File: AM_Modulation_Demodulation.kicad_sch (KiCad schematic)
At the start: 33 parts, among them U1 LM1496H, U2 TL082

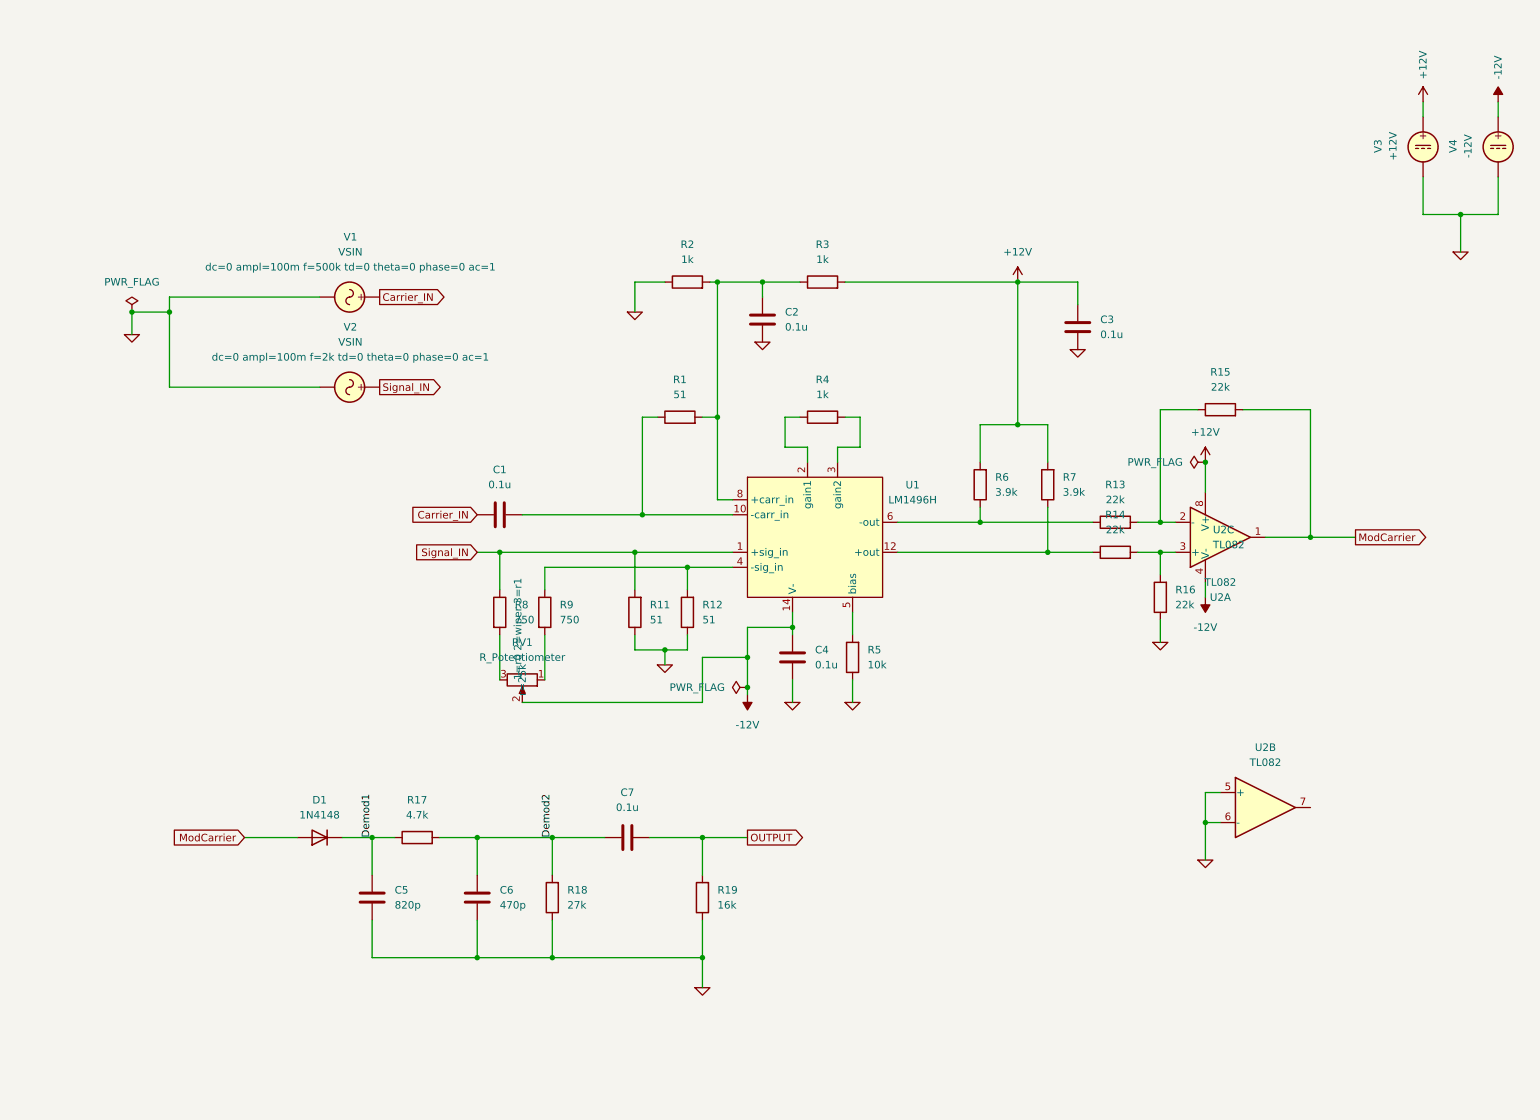
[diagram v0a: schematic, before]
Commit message: Rearranged Schematic. Fixed Readme
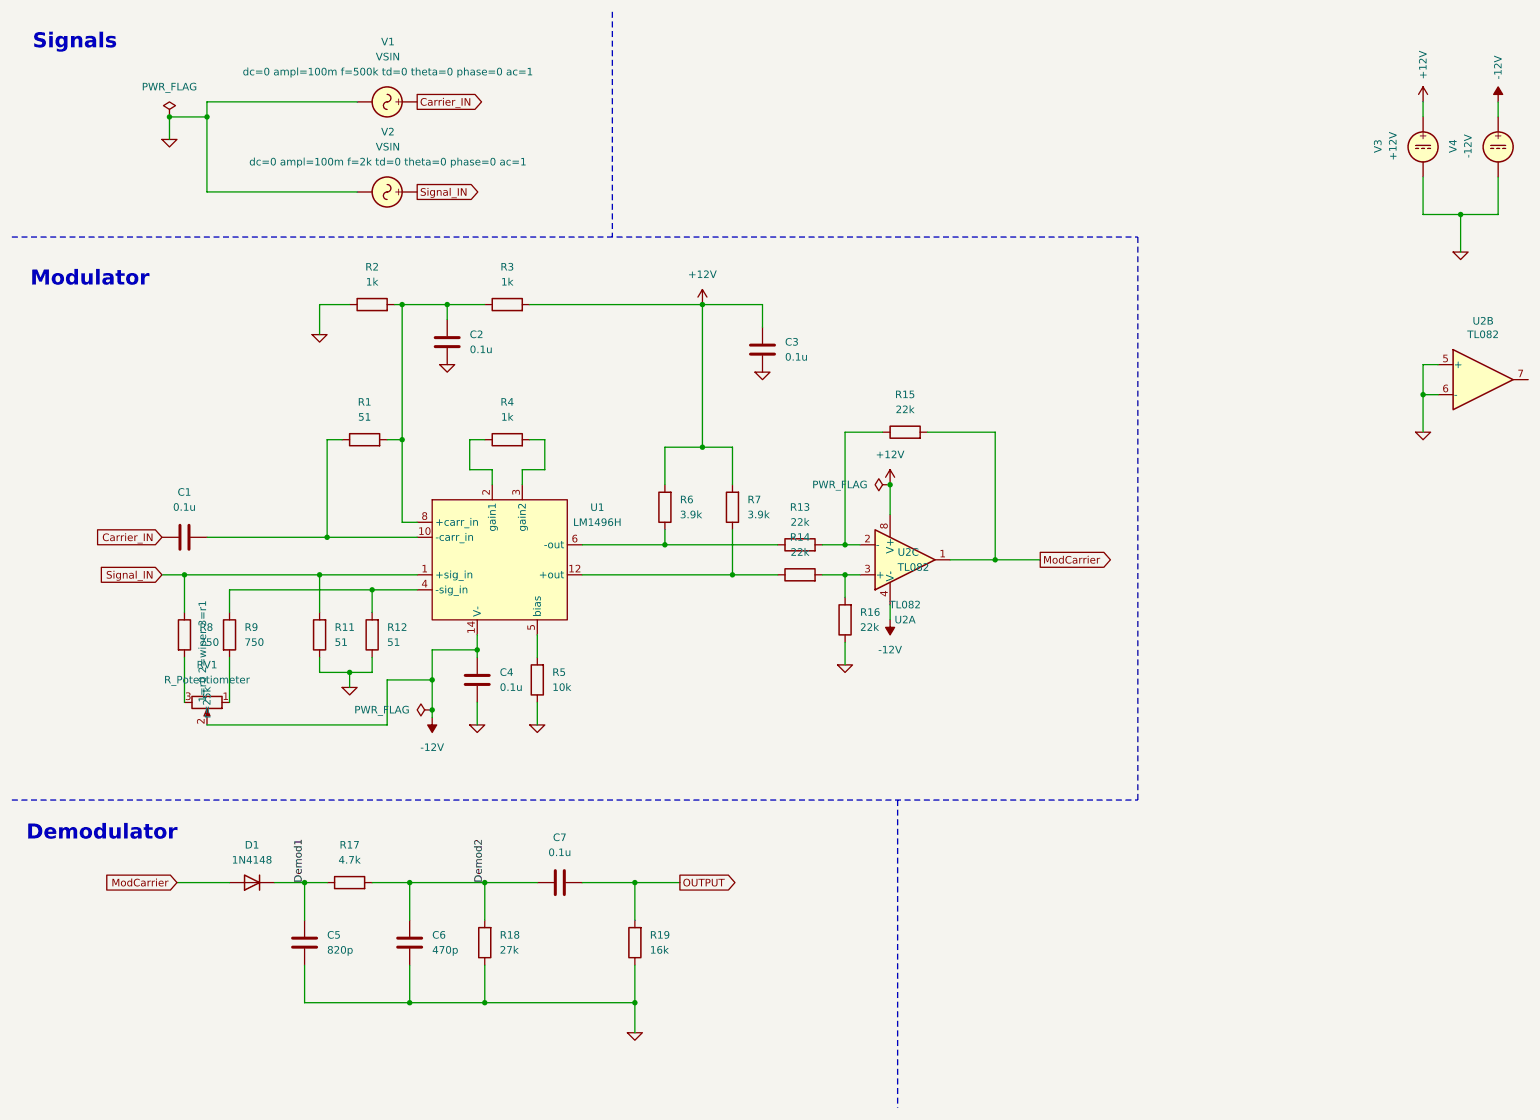
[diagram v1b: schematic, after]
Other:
- note added: "Demodulator"
- note added: "Modulator"
- note added: "Signals"
- moved on the sheet: C1, C2, C3, C4, C5, C6, C7, D1, R1, R11, R12, R13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
